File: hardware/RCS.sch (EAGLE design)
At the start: 60 parts, among them U1 LT1930, U2 TD62083AFNG, U3 HX711, U4 HX711

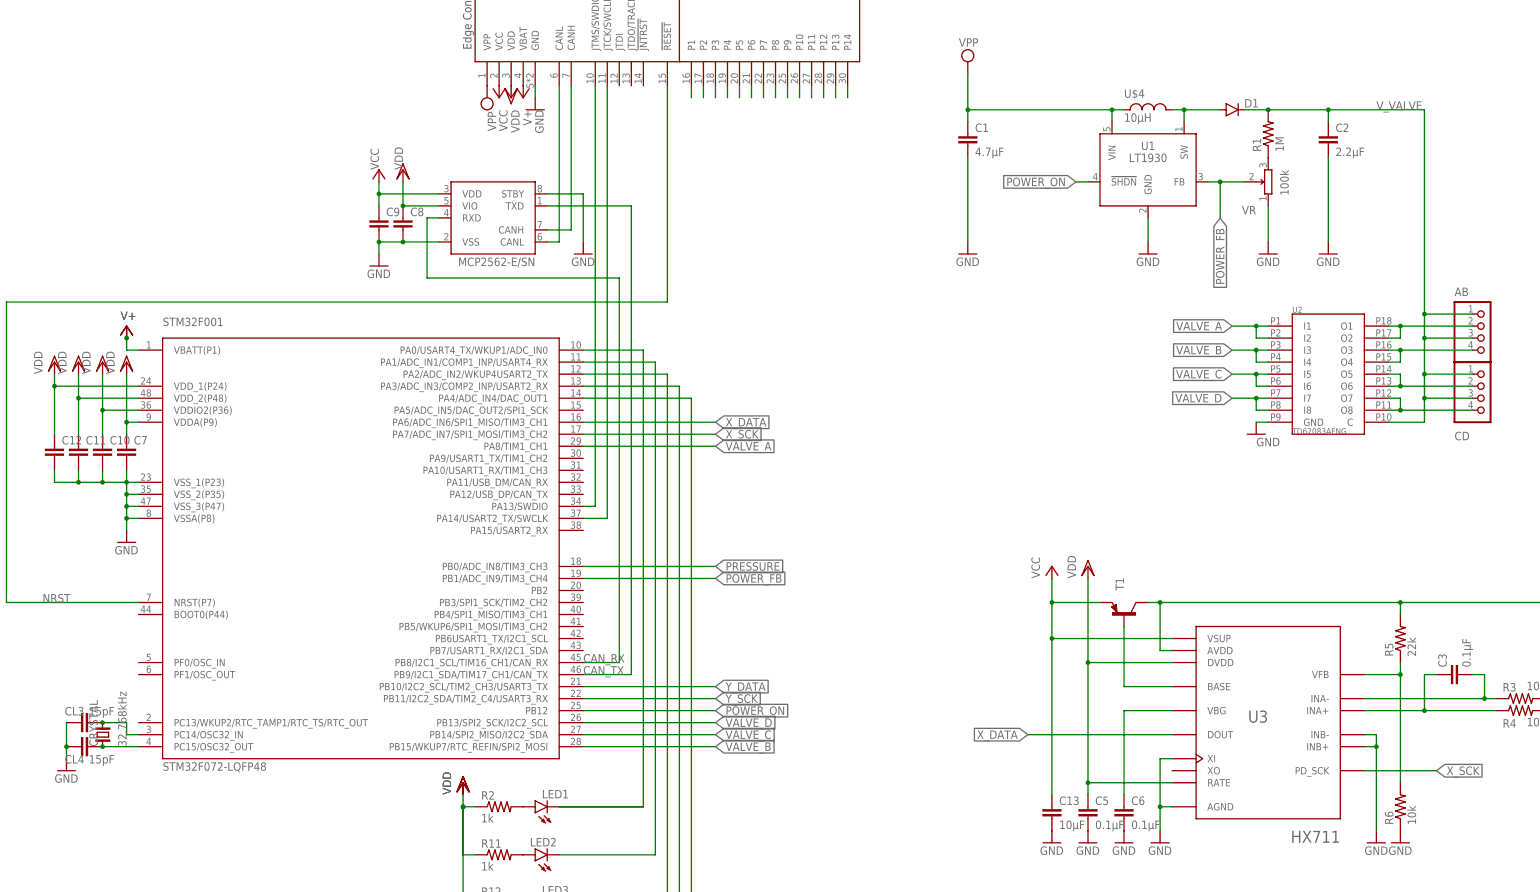
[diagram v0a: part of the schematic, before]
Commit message: RCS基板を追加
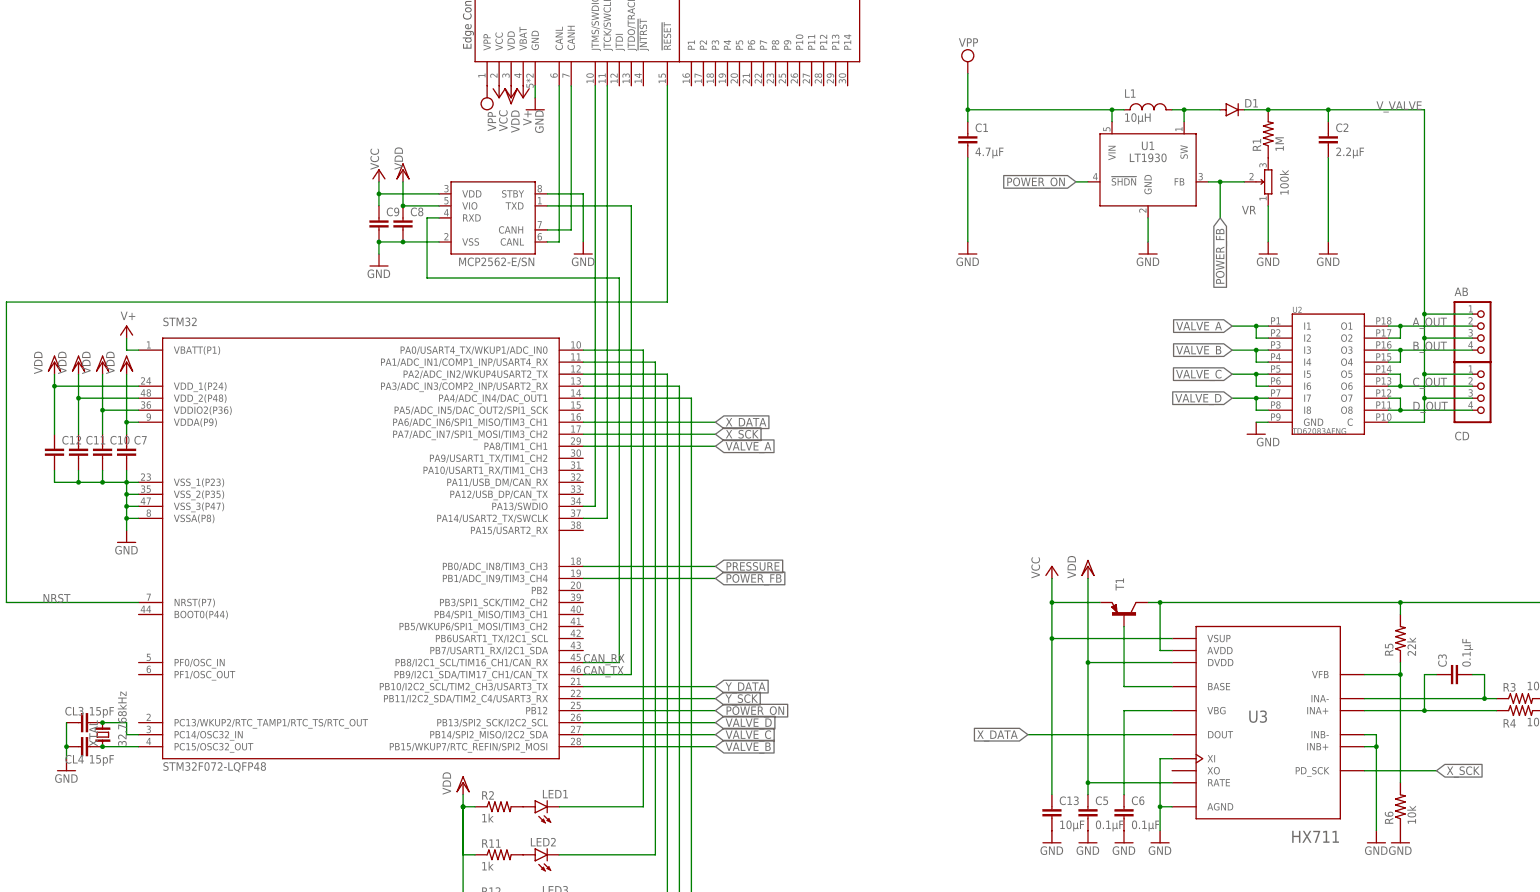
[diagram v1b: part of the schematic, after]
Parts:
- renumbered CRYSTAL to XTAL, STM32F001 to STM32, U$4 to L1
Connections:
- net N$10 renamed D_OUT
- net N$12 renamed A_OUT
- net N$8 renamed B_OUT
- net N$9 renamed C_OUT
- removed net N$24: U$2.P14
- removed net N$28: STM32.PA0/USART4_TX/WKUP1/ADC_IN0
- removed net N$33: U$2.P13
- removed net N$34: U$2.P12
- removed net N$35: U$2.P11
- removed net N$36: U$2.P10
- removed net N$43: U$2.P9
- removed net N$44: U$2.P8
- removed net N$45: U$2.P7
- removed net N$46: U$2.P6
- removed net N$47: U$2.P5
- removed net N$48: U$2.P4
- removed net N$49: U$2.P3
- removed net N$72: U$2.P1
- removed net N$73: U$2.P2
- net N$51: now also STM32.PA0/USART4_TX/WKUP1/ADC_IN0

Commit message: 気圧センサ用ポートを追加
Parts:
- removed PRESSURE: B3B-ZR, jst:B3B-ZR
- added C20: (no value), rcl:C-EUC0603
- added PRES1, PRES2: B3B-ZR, jst:B3B-ZR
- added R17: 10k, rcl:R-US_R0603
- added R18: 15k, rcl:R-US_R0603
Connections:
- net PRESSURE renamed PRESSURE_1
- new net N$8: PRES2.3, R17.2
- new net PRESSURE_2: R17.1, R18.2, STM32.PA5/ADC_IN5/DAC_OUT2/SPI1_SCK
- net GND: now also C20.2, PRES1.2, PRES2.2, R18.1; no longer PRESSURE.2
- net N$17: now also PRES1.3; no longer PRESSURE.3
- net VCC: now also C20.1, PRES1.1, PRES2.1; no longer PRESSURE.1
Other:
- moved on the sheet: C19, R15, R16
